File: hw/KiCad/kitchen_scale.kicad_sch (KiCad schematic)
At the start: 6 parts, among them J1 Conn_01x11_TFT_DEBO, J2 Conn_HX711, SW1 SW_SPDT, U1 DEBO1_3_7LI_1_0A_charge_contr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

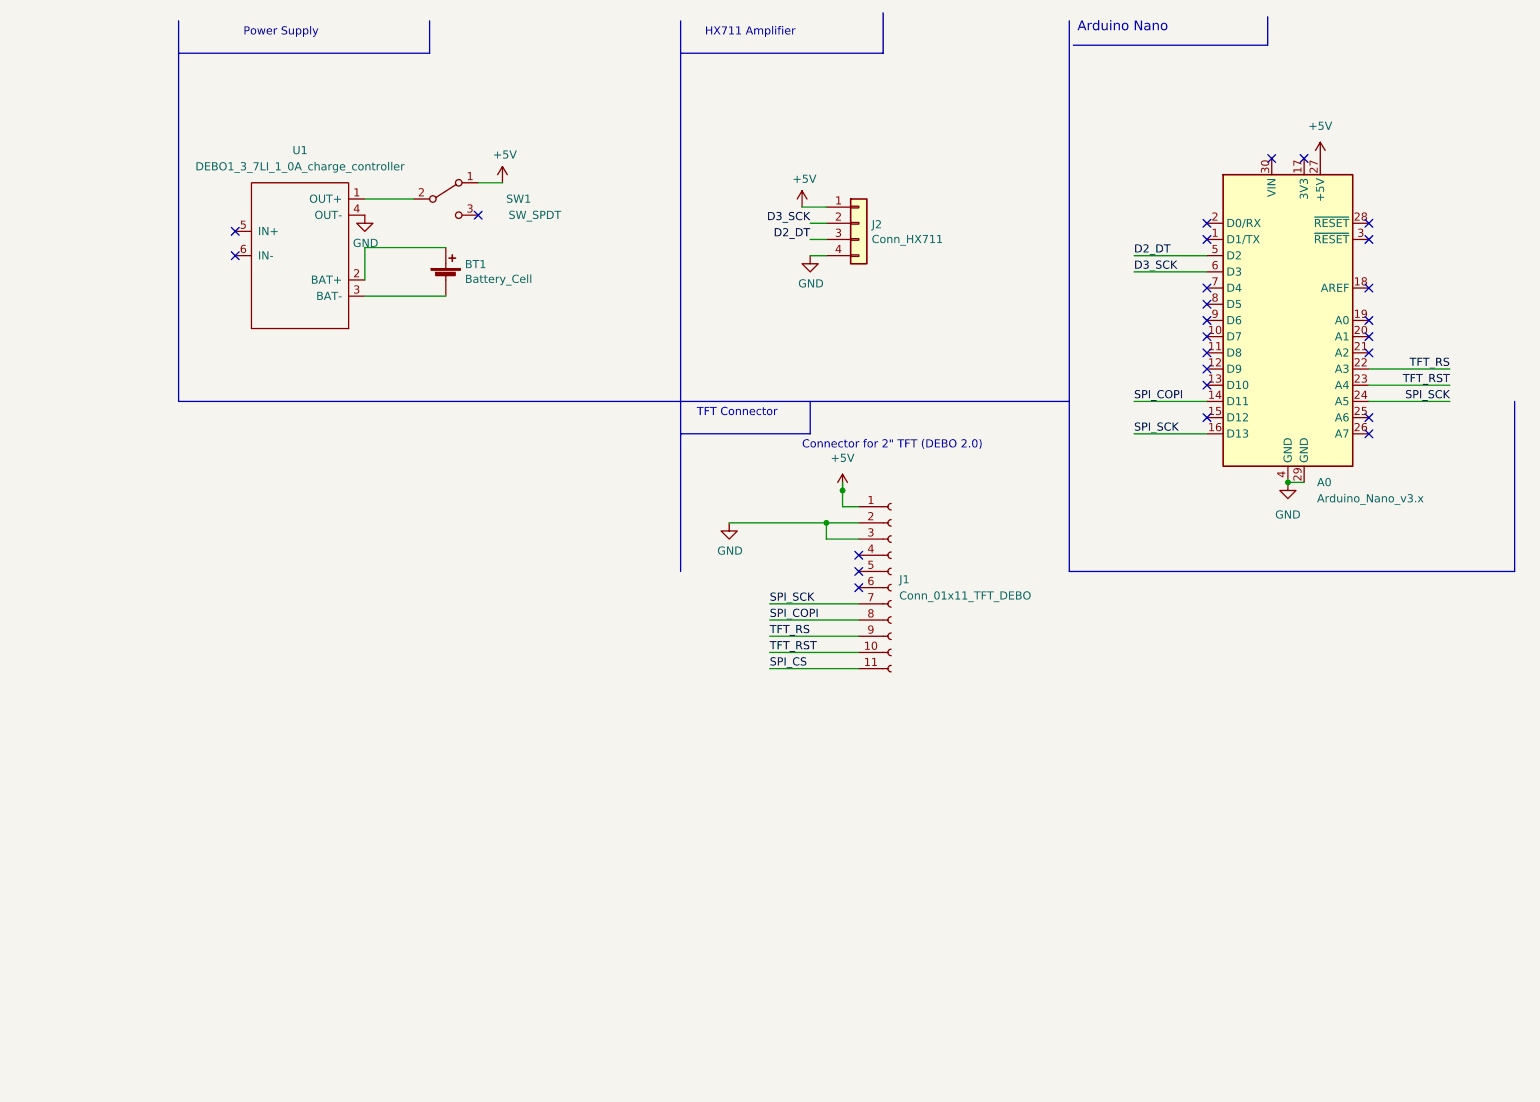
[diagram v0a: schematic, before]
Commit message: Change to ESP8266, as needing anyway 3.3V and is smaller.
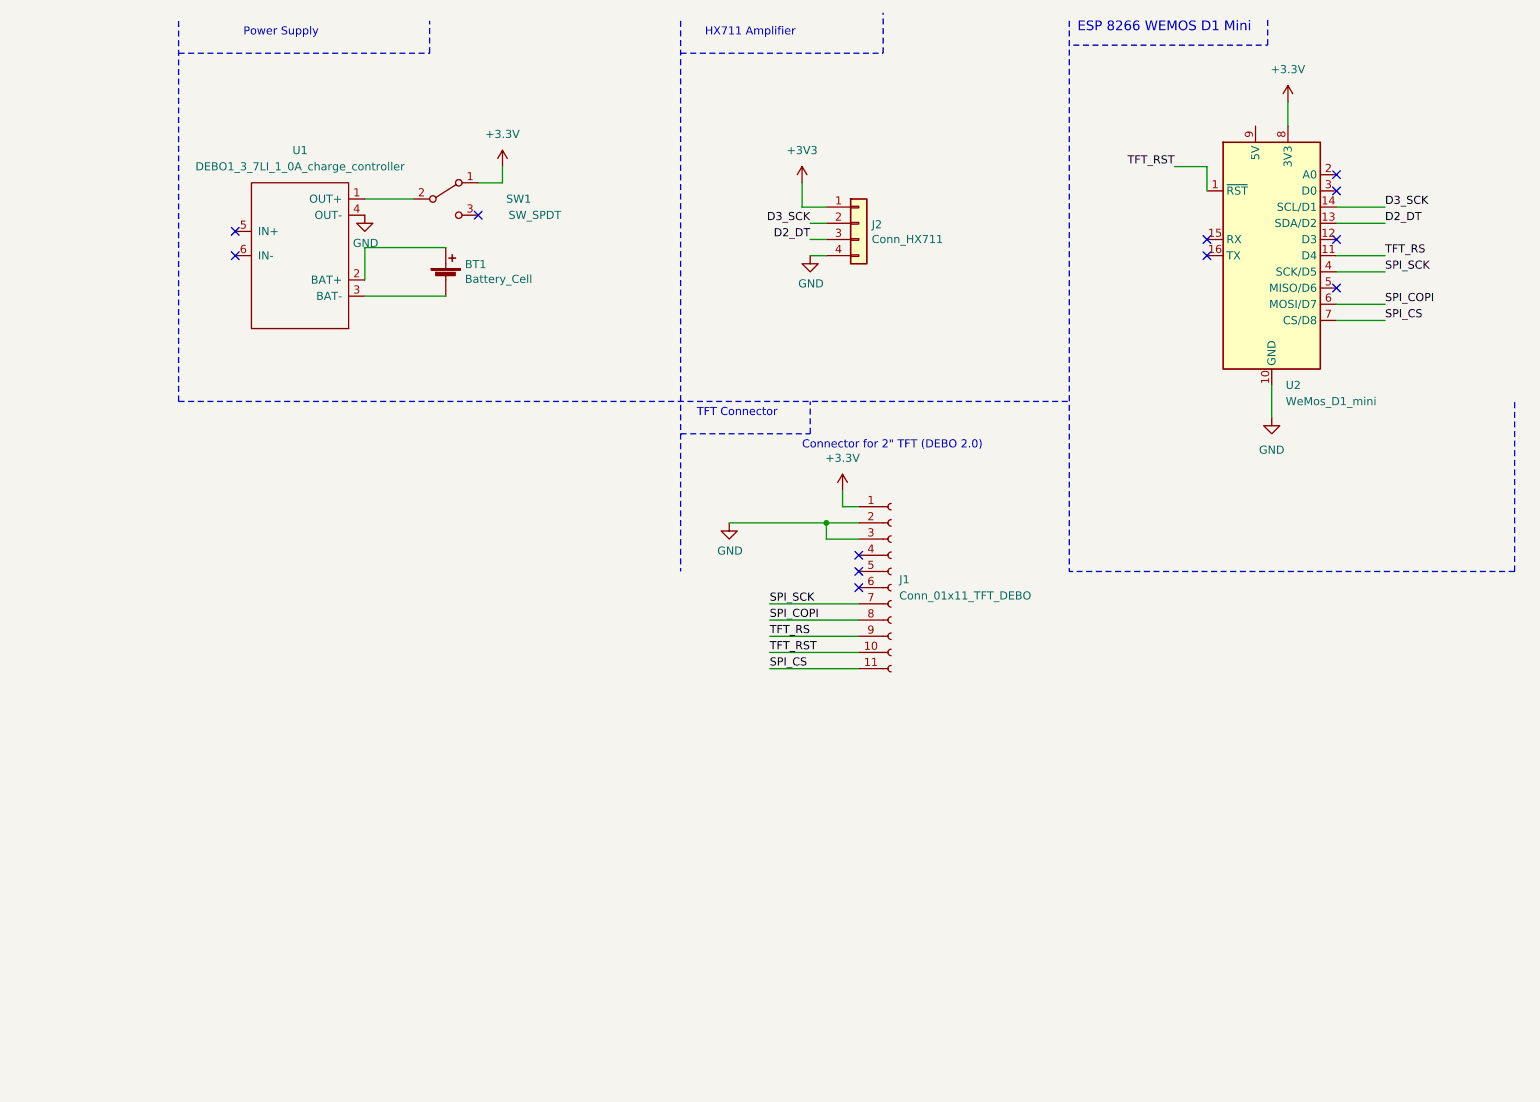
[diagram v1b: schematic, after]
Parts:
- removed A0: Arduino_Nano_v3.x, Module:Arduino_Nano, symbol MCU_Module:Arduino_Nano_v3.x
- added U2: WeMos_D1_mini, Module:WEMOS_D1_mini_light, symbol MCU_Module:WeMos_D1_mini
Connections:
- net D2_DT: now also U2.13 (SDA/D2)
- net D3_SCK: now also U2.14 (SCL/D1)
- net GND: now also U2.10 (GND)
- net SPI_COPI: now also U2.6 (MOSI/D7)
- net SPI_CS: now also U2.7 (CS/D8)
- net SPI_SCK: now also U2.4 (SCK/D5)
- net TFT_RS: now also U2.11 (D4)
- net TFT_RST: now also U2.1 (~{RST})
- net +5V renamed +3.3V
- net +3.3V: now also U2.8 (3V3); no longer J2.1 (Pin_1)
- new net +3V3: J2.1 (Pin_1)
- no-connect marks 26 -> 12
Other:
- note added: "ESP 8266 WEMOS D1 Mini"
- note removed: "Arduino Nano"

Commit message: Clean up of symbols, added Mine Added buttons and battery charging state
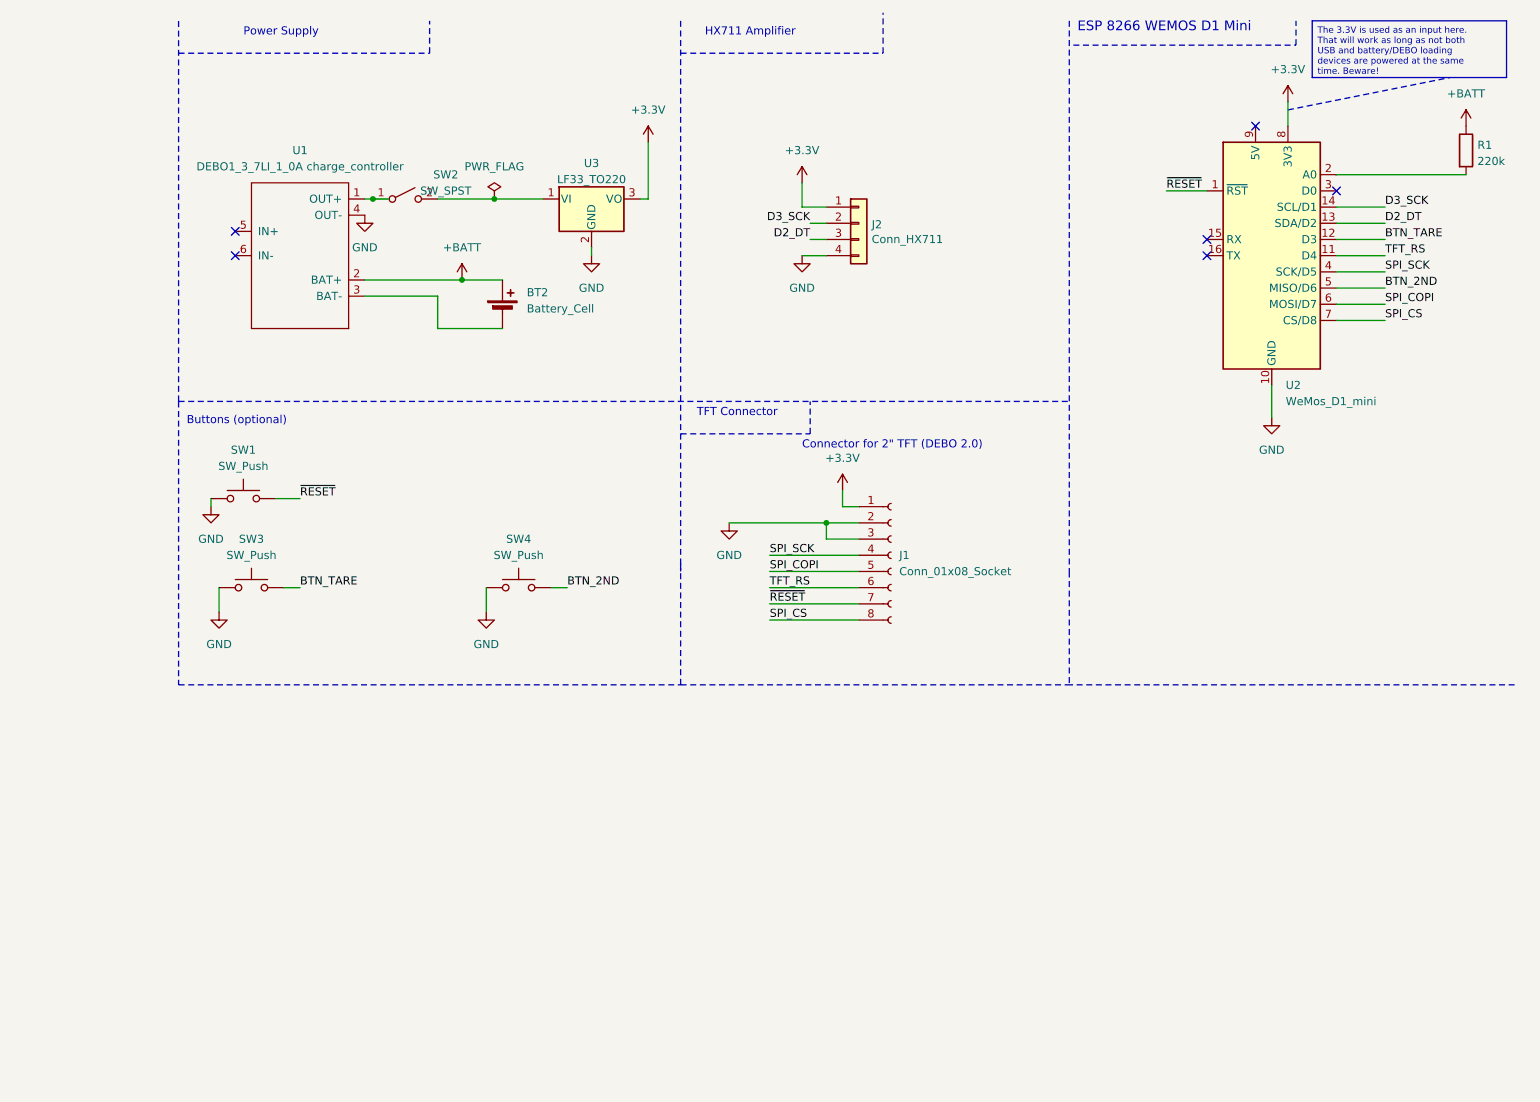
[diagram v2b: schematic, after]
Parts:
- removed BT1: Battery_Cell, symbol Device:Battery_Cell
- removed J1: Conn_01x11_TFT_DEBO, symbol Connector:Conn_01x11_Female
- removed SW1: SW_SPDT, symbol Switch:SW_SPDT
- removed U2: WeMos_D1_mini, Module:WEMOS_D1_mini_light, symbol MCU_Module:WeMos_D1_mini
- added BT2: Battery_Cell, symbol Device:Battery_Cell
- added J1: Conn_01x08_Socket, symbol Connector:Conn_01x08_Socket
- added R1: 220k, Resistor_THT:R_Axial_DIN0207_L6.3mm_D2.5mm_P7.62mm_Horizontal, symbol Device:R
- added SW1, SW3, SW4: SW_Push, symbol Switch:SW_Push
- added SW2: SW_SPST, symbol Switch:SW_SPST
- added U2: WeMos_D1_mini, Module:WEMOS_D1_mini_light, symbol Mine:WeMos_D1_mini
- added U3: LF33_TO220, Package_TO_SOT_THT:TO-220-3_Vertical, symbol Regulator_Linear:LF33_TO220
- U1: value DEBO1_3_7LI_1_0A_charge_controller -> DEBO1_3_7LI_1_0A charge_controller
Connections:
- net +3V3 is gone; now on net +3.3V: J2.1 (Pin_1)
- net +3.3V: now also J1.1 (Pin_1), U2.8 (3V3), U3.3 (VO)
- net D2_DT: now also U2.13 (SDA/D2)
- net D3_SCK: now also U2.14 (SCL/D1)
- net GND: now also J1.2 (Pin_2), J1.3 (Pin_3), SW1.1, SW3.1, SW4.1, U2.10 (GND), U3.2 (GND)
- net SPI_COPI: now also J1.5 (Pin_5), U2.6 (MOSI/D7)
- net SPI_CS: now also J1.8 (Pin_8), U2.7 (CS/D8)
- net SPI_SCK: now also J1.4 (Pin_4), U2.4 (SCK/D5)
- net TFT_RS: now also J1.6 (Pin_6), U2.11 (D4)
- net +BATT: now reaches U1.2 (BAT+)
- net +BATT: now also BT2.1 (+), R1.1
- net at U1.3 (BAT-): now also BT2.2 (-)
- net at U1.1 (OUT+): now also SW2.1 (A)
- new net: R1.2, U2.2 (A0)
- new net: SW2.2 (B), U3.1 (VI)
- new net BTN_2ND: SW4.2, U2.5 (MISO/D6)
- new net BTN_TARE: SW3.2, U2.12 (D3)
- new net ~{RESET}: J1.7 (Pin_7), SW1.2, U2.1 (~{RST})
- no-connect marks 12 -> 6
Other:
- note added: "Buttons (optional)"
